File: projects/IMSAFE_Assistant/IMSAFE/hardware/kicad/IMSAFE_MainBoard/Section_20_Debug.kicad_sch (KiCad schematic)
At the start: 0 parts

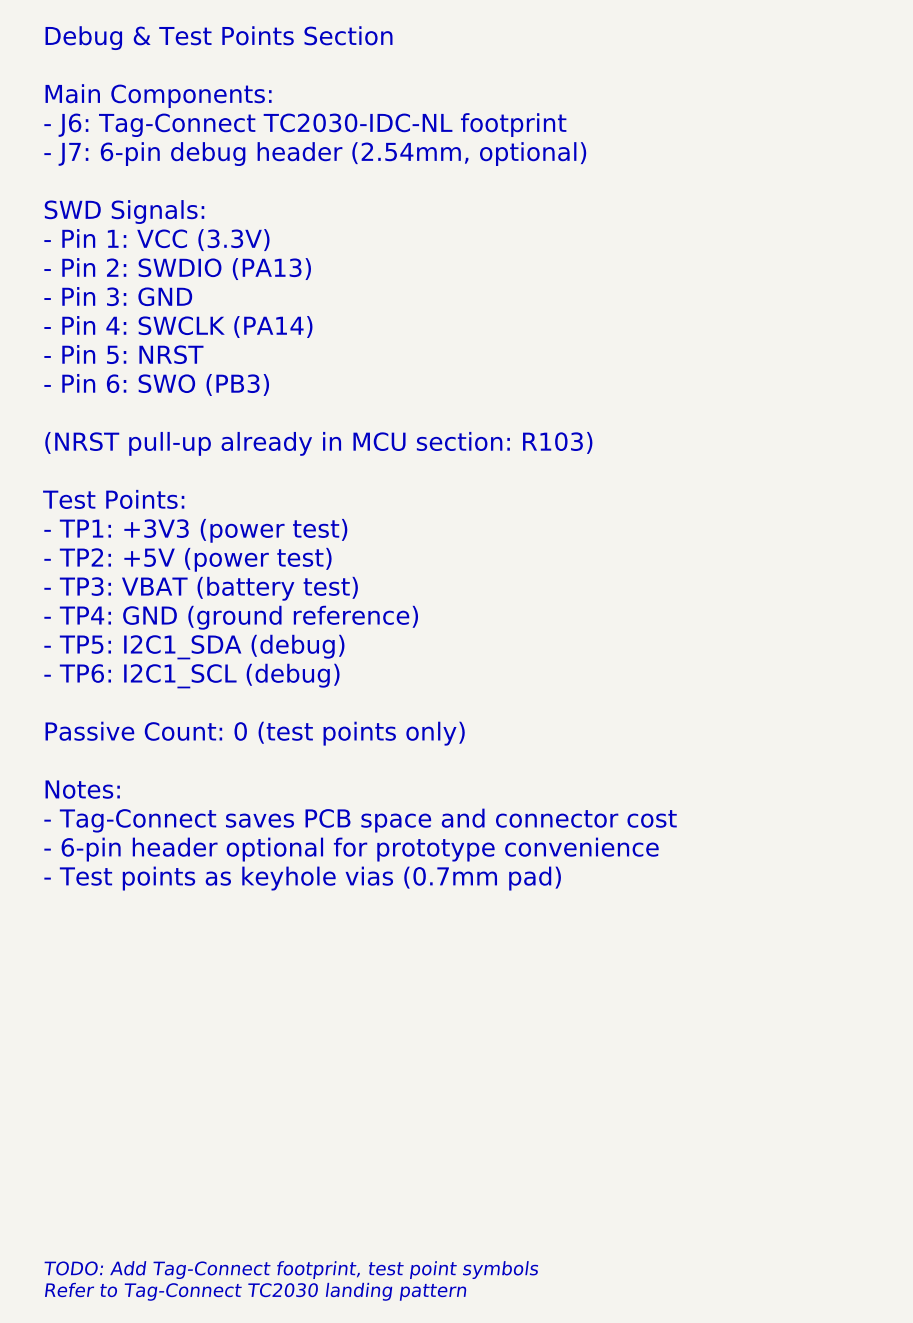
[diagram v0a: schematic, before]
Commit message: Update KiCad schematics and add analysis files
- Update all MainBoard schematic sections with component placement
- Add ERC reports and analysis scripts for schematic validation
- Update Radar Interface and SwitchLED Board projects
- Sync KiCad project files with latest session changes

Co-Authored-By: Claude Opus 4.5 <noreply@anthropic.com>
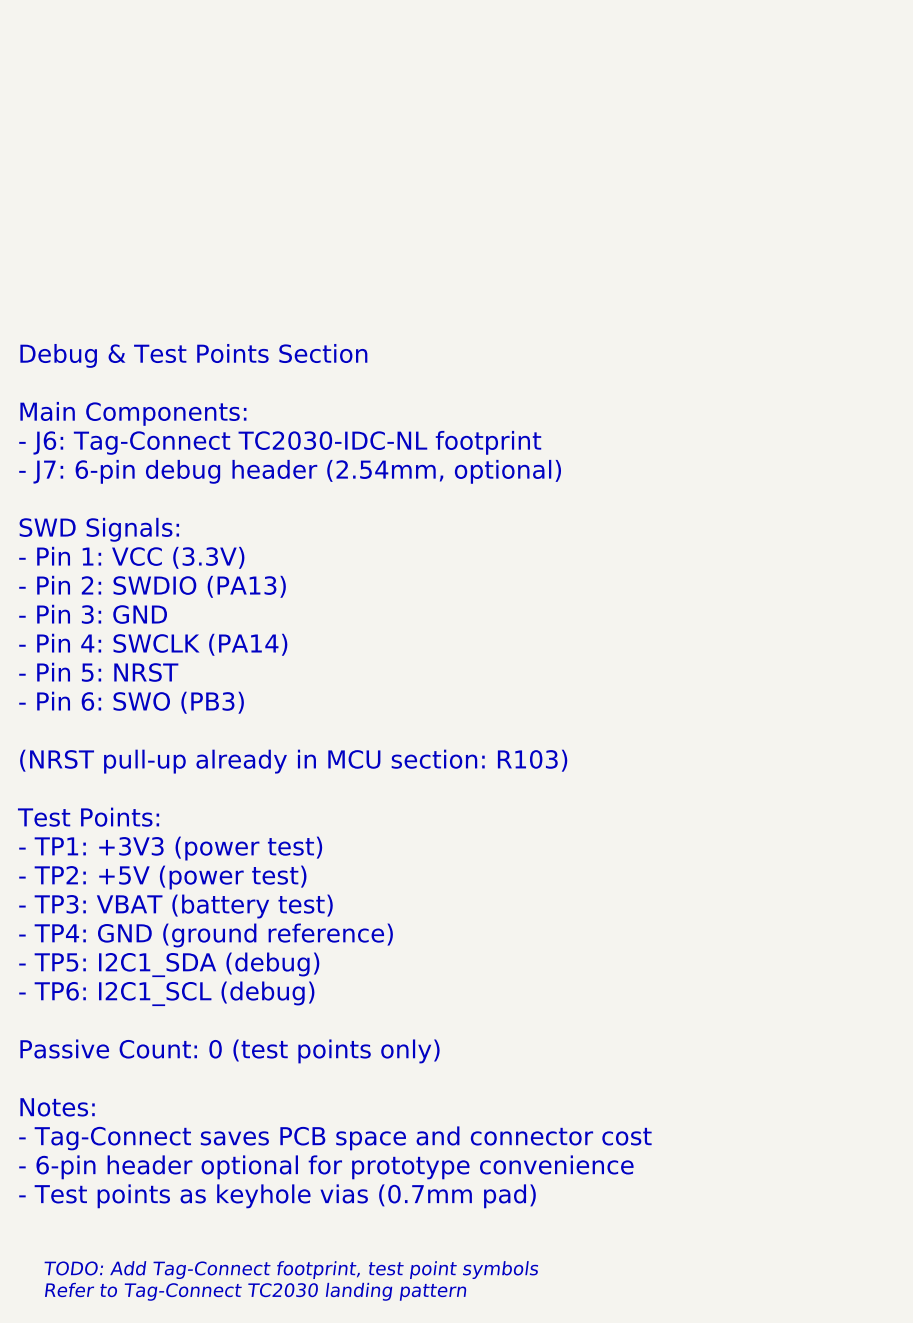
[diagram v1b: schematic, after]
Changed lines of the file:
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@@
 (kicad_sch
-	(version 20231120)
+	(version 20250114)
 	(generator "eeschema")
-	(generator_version "8.0")
-	(uuid "sec20-0001-0002-0003-000000000001")
+	(generator_version "9.0")
 	(paper "A4")
 	(title_block
@@
 	(text "Debug & Test Points Section\n\nMain Components:\n- J6: Tag-Connect TC2030-IDC-NL footprint\n- J7: 6-pin debug header (2.54mm, optional)\n\nSWD Signals:\n- Pin 1: VCC (3.3V)\n- Pin 2: SWDIO (PA13)\n- Pin 3: GND\n- Pin 4: SWCLK (PA14)\n- Pin 5: NRST\n- Pin 6: SWO (PB3)\n\n(NRST pull-up already in MCU section: R103)\n\nTest Points:\n- TP1: +3V3 (power test)\n- TP2: +5V (power test)\n- TP3: VBAT (battery test)\n- TP4: GND (ground reference)\n- TP5: I2C1_SDA (debug)\n- TP6: I2C1_SCL (debug)\n\nPassive Count: 0 (test points only)\n\nNotes:\n- Tag-Connect saves PCB space and connector cost\n- 6-pin header optional for prototype convenience\n- Test points as keyhole vias (0.7mm pad)"
 		(exclude_from_sim no)
-		(at 25.4 25.4 0)
+		(at 22.606 60.706 0)
 		(effects
 			(font
@@
 			(justify left)
 		)
-		(uuid "sec20-text-001")
 	)
 	(text "TODO: Add Tag-Connect footprint, test point symbols\nRefer to Tag-Connect TC2030 landing pattern"
@@
 			(justify left)
 		)
-		(uuid "sec20-todo-001")
 	)
 )
